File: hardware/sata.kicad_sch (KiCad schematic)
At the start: 36 parts, among them IC1 ASM1061, J9 SATA_22pin, Q2 FDS4435BZ, Q3 FDS4435BZ, Q5 2N7002, Q6 2N7002, Y1 25MHz

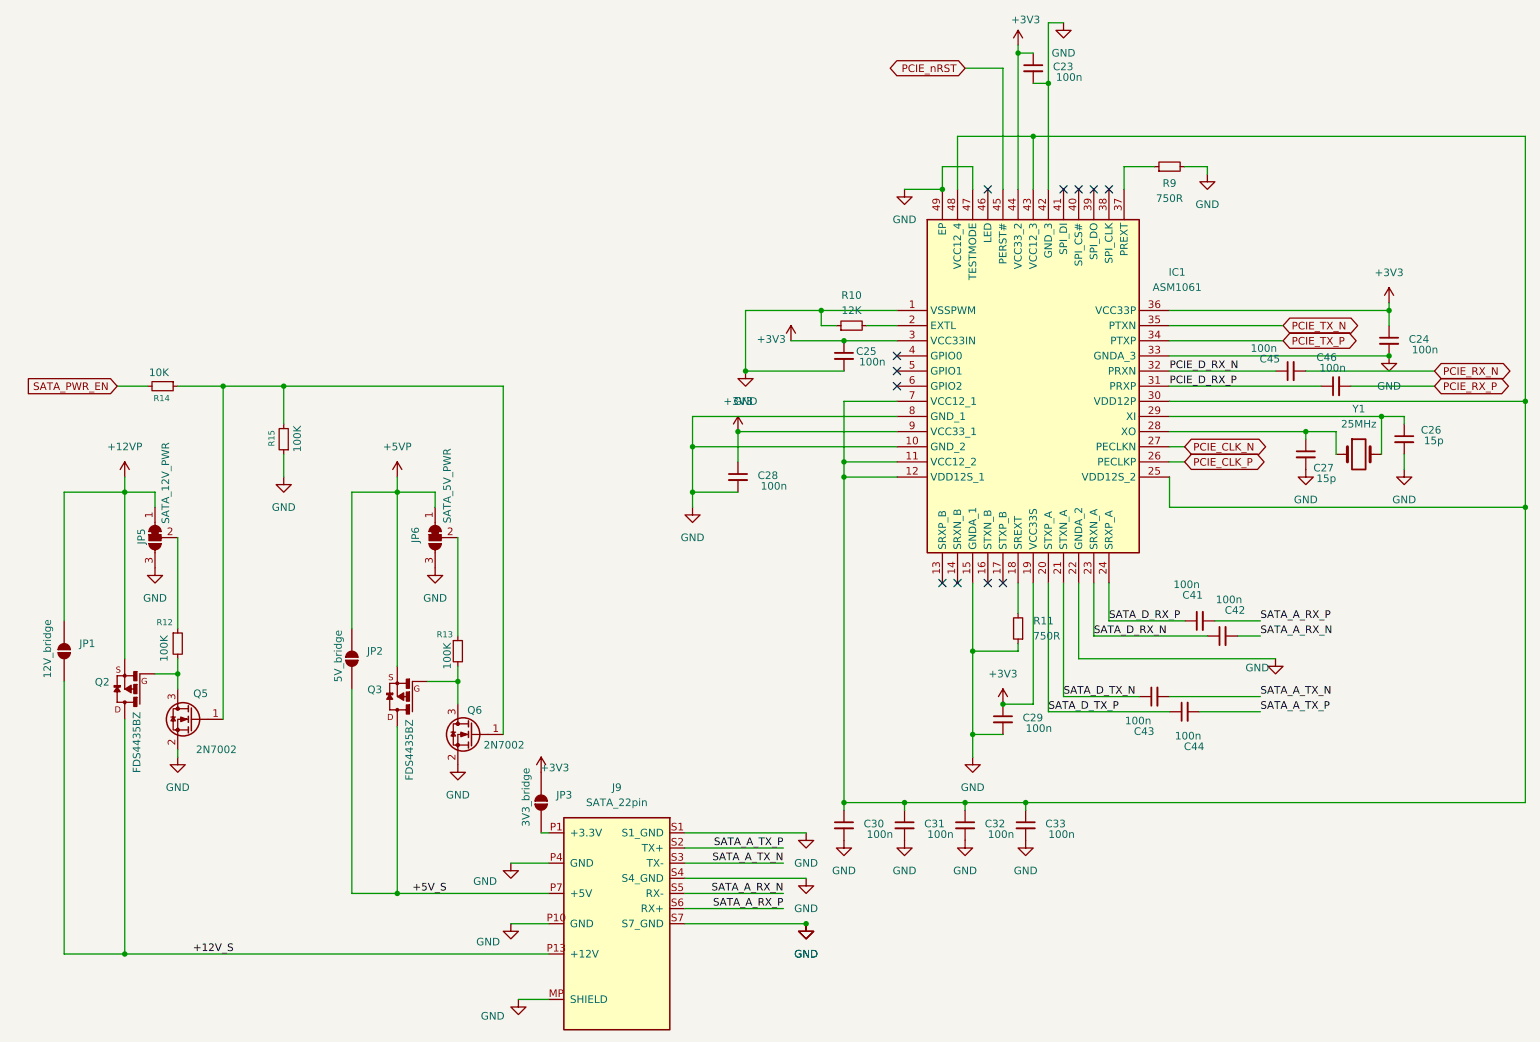
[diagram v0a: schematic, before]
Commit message: refactor: reannotate PCB by position + rename IC1 to U prefix
All reference designators renumbered top-to-bottom, left-to-right.
ASM1061 changed from IC to U prefix.
ERC: 0 errors. DRC: 0 violations. Parity: 0 issues.
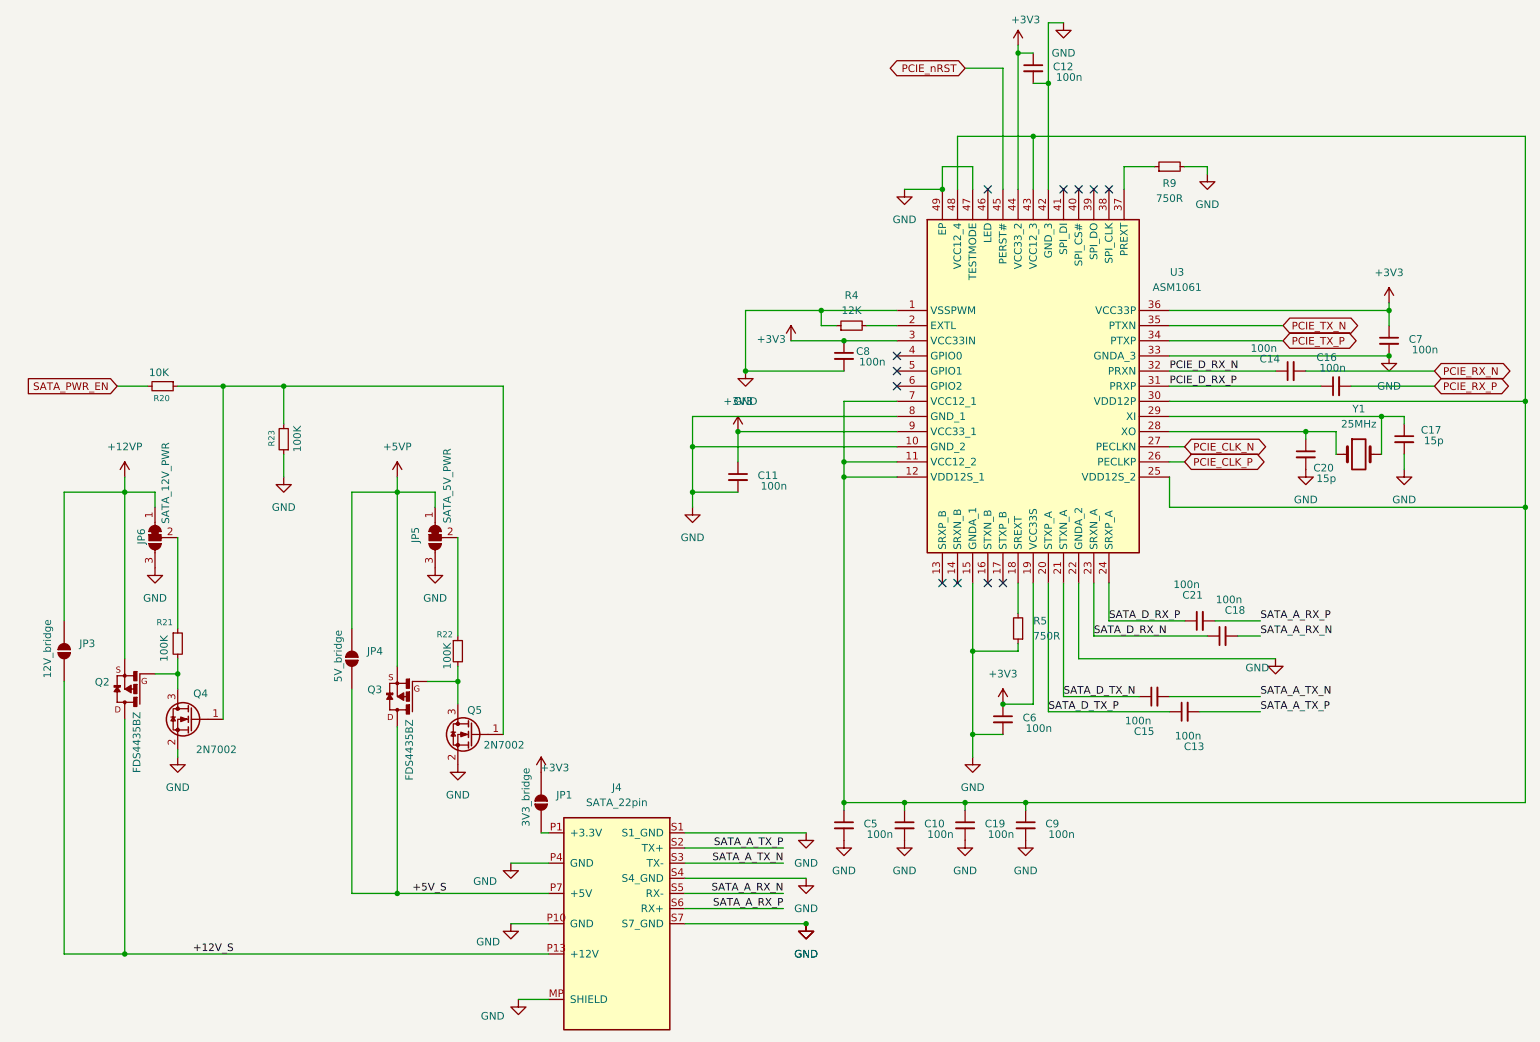
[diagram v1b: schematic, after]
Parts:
- C10: renamed from C31; KiLib_Generator (none) -> SMD_2terminal_chip_molded
- C11: renamed from C28; KiLib_Generator (none) -> SMD_2terminal_chip_molded
- C12: renamed from C23; KiLib_Generator (none) -> SMD_2terminal_chip_molded
- C13: renamed from C44; KiLib_Generator (none) -> SMD_2terminal_chip_molded
- C14: renamed from C45; KiLib_Generator (none) -> SMD_2terminal_chip_molded
- C15: renamed from C43; KiLib_Generator (none) -> SMD_2terminal_chip_molded
- C16: renamed from C46; KiLib_Generator (none) -> SMD_2terminal_chip_molded
- C17: renamed from C26; KiLib_Generator (none) -> SMD_2terminal_chip_molded
- C18: renamed from C42; KiLib_Generator (none) -> SMD_2terminal_chip_molded
- C19: renamed from C32; KiLib_Generator (none) -> SMD_2terminal_chip_molded
- C20: renamed from C27; KiLib_Generator (none) -> SMD_2terminal_chip_molded
- C21: renamed from C41; KiLib_Generator (none) -> SMD_2terminal_chip_molded
- C5: renamed from C30; KiLib_Generator (none) -> SMD_2terminal_chip_molded
- C6: renamed from C29; KiLib_Generator (none) -> SMD_2terminal_chip_molded
- C7: renamed from C24; KiLib_Generator (none) -> SMD_2terminal_chip_molded
- C8: renamed from C25; KiLib_Generator (none) -> SMD_2terminal_chip_molded
- C9: renamed from C33; KiLib_Generator (none) -> SMD_2terminal_chip_molded
- Q4: renamed from Q5; KiLib_Generator (none) -> package/gullwing
- Q5: renamed from Q6; KiLib_Generator (none) -> package/gullwing
- R20: renamed from R14; KiLib_Generator (none) -> SMD_2terminal_chip_molded
- R21: renamed from R12; KiLib_Generator (none) -> SMD_2terminal_chip_molded
- R22: renamed from R13; KiLib_Generator (none) -> SMD_2terminal_chip_molded
- R23: renamed from R15; KiLib_Generator (none) -> SMD_2terminal_chip_molded
- R4: renamed from R10; KiLib_Generator (none) -> SMD_2terminal_chip_molded
- R5: renamed from R11; KiLib_Generator (none) -> SMD_2terminal_chip_molded
- R9: KiLib_Generator (none) -> SMD_2terminal_chip_molded
- renumbered J9 to J4, JP3 to JP1, JP1 to JP3, JP2 to JP4, JP6 to JP5, JP5 to JP6, IC1 to U3

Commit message: feat: add InvenTree IPN field to all schematic symbols
102 components mapped to 41 unique InvenTree part numbers.
IPN format: category prefix + sequential number (e.g. C-001, R-002, U-009).
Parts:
- C10, C11, C12, C13, C14, C15, C16, C18, C19, C21, C5, C6, C7, C8, C9: IPN (none) -> C-001
- C17, C20: IPN (none) -> C-002
- J4: IPN (none) -> J-007
- Q2, Q3: IPN (none) -> Q-001
- Q4, Q5: IPN (none) -> Q-003
- R20: IPN (none) -> R-002
- R21, R22, R23: IPN (none) -> R-004
- R4: IPN (none) -> R-007
- R5, R9: IPN (none) -> R-020
- U3: IPN (none) -> U-009
- Y1: IPN (none) -> Y-003

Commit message: chore: remove redundant supplier fields, keep IPN as single link to InvenTree
Removed: Supplier, Digikey, Notes, KiLib_Generator, Mouser, Arrow fields.
InvenTree IPN is now the only external reference in the schematic.
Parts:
- C10, C11, C12, C13, C14, C15, C16, C17, C18, C19, C20, C21, C5, C6, C7, C8, C9: Digikey 1276-1180-1-ND -> (none); KiLib_Generator SMD_2terminal_chip_molded -> (none); Notes 10% 16V Ceramic Capacitor X7R -> (none); Supplier https://www.digikey.ch/de/products/detail/samsung-electro-m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 -> (none)
- Q2, Q3: IPN Q-001 -> (none); Supplier https://www.digikey.ch/de/products/detail/onsemi/FDS4435BZ/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 -> (none)
- Q4, Q5: IPN Q-003 -> (none); KiLib_Generator package/gullwing -> (none)
- R20, R21, R22, R23, R4, R5, R9: KiLib_Generator SMD_2terminal_chip_molded -> (none)
- U3: IPN U-009 -> (none)

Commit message: feat: complete IPN assignment for all BOM parts
All components now have InvenTree IPN field.
Added IPN to granit library symbols (ASM1061, FDS4435BZ, AP64501).
Added Q-003 to 2N7002 instances.
Only TestPoints have no IPN (not purchaseable).
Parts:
- Q2, Q3: IPN (none) -> Q-001
- Q4, Q5: IPN (none) -> Q-003
- U3: IPN (none) -> U-009
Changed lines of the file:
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@@
 			)
 		)
+		(property "IPN" "Q-003"
+			(at 88.9 135.89 0)
+			(hide yes)
+			(show_name no)
+			(do_not_autoplace no)
+			(effects
+				(font
+					(size 1.27 1.27)
+				)
+			)
+		)
 		(pin "2"
 		)
@@
 			)
 		)
+		(property "IPN" "Q-001"
+			(at 76.2 129.54 0)
+			(hide yes)
+			(show_name no)
+			(do_not_autoplace no)
+			(effects
+				(font
+					(size 1.27 1.27)
+				)
+			)
+		)
 		(pin "1-3"
 		)
@@
 			)
 		)
+		(property "IPN" "U-009"
+			(at 160.02 64.77 0)
+			(hide yes)
+			(show_name no)
+			(do_not_autoplace no)
+			(effects
+				(font
+					(size 1.27 1.27)
+				)
+			)
+		)
 		(pin "26"
 		)
@@
 			)
 		)
+		(property "IPN" "Q-001"
+			(at 30.48 128.27 0)
+			(hide yes)
+			(show_name no)
+			(do_not_autoplace no)
+			(effects
+				(font
+					(size 1.27 1.27)
+				)
+			)
+		)
 		(pin "5-8"
 		)
@@
 			(at 41.91 133.35 0)
 			(hide yes)
+			(show_name no)
+			(do_not_autoplace no)
+			(effects
+				(font
+					(size 1.27 1.27)
+				)
+			)
+		)
+		(property "IPN" "Q-003"
+			(at 41.91 133.35 0)
+			(hide yes)

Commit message: fix: restore SATA TX+ pin number to S2 (was corrupted by HR911130A shield pin remap)
ERC: 0 errors, 0 warnings
DRC: 0 violations, 0 parity issues
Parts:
- J4: IPN J-007 -> (none)
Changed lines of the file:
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@@
-			)
-		)
-		(property "IPN" "J-007"
-			(at 0 0 0)
-			(hide yes)
-			(show_name no)
-			(do_not_autoplace no)
-			(effects
-				(font
-					(size 1.27 1.27)
-				)
 			)
 		)
@@
 		(pin "P4"
 		)
-		(pin "S2"
+		(pin "S1"
 		)
 		(pin "S3"
@@
 		(pin "P15"
 		)
-		(pin "S1"
+		(pin "S2"
 		)
 		(pin "P3"

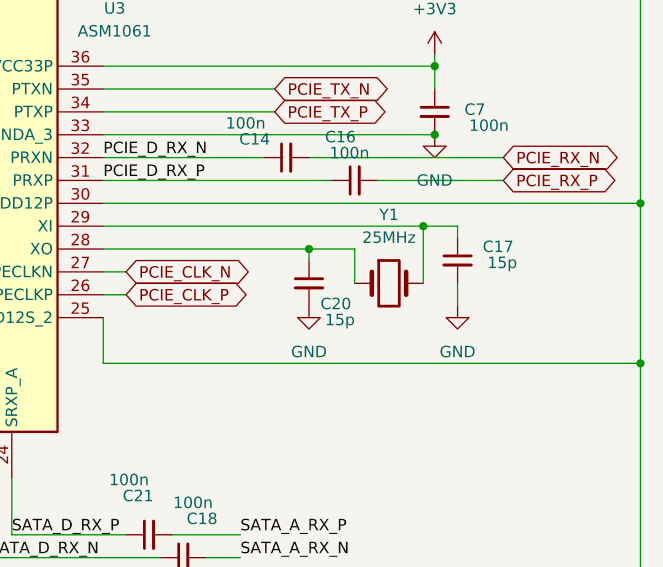
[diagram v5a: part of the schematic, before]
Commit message: feat: swap crystal Y1 to 2016 4-pin (easier to source)
Changed from Crystal_SMD_3215-2Pin to Crystal_SMD_2016-4Pin_2.0x1.6mm.
Re-routed PCIe area around new crystal placement.
ERC: 0 errors, 0 warnings. DRC: 0 violations.
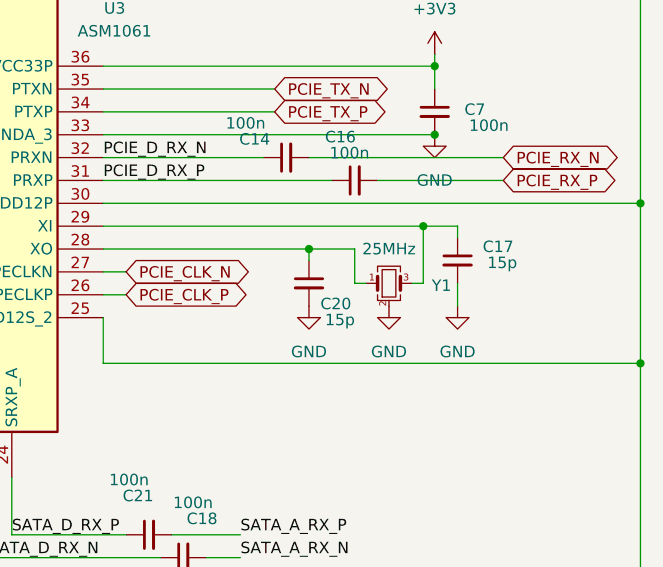
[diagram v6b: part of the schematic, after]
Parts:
- removed Y1: 25MHz, Crystal:Crystal_SMD_3215-2Pin_3.2x1.5mm, symbol Device:Crystal
- added Y1: 25MHz, Crystal:Crystal_SMD_2016-4Pin_2.0x1.6mm, symbol Device:Crystal_GND24_Small
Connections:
- net GND: now also Y1.2 (G), Y1.4 (G)
- net at C17.1, U3.29 (XI): now also Y1.3
- net at C20.1, U3.28 (XO): now also Y1.1
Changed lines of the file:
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@@
 	(wire
 		(pts
+			(xy 233.68 88.9) (xy 234.95 88.9)
+		)
+		(stroke
+			(width 0)
+			(type default)
+		)
+	)
+	(wire
+		(pts
 			(xy 161.29 147.32) (xy 151.13 147.32)
 		)
@@
 	(wire
 		(pts
+			(xy 240.03 88.9) (xy 241.3 88.9)
+		)
+		(stroke
+			(width 0)
+			(type default)
+		)
+	)
+	(wire
+		(pts
 			(xy 265.43 80.01) (xy 265.43 97.79)
 		)
@@
 	)
 	(symbol
-		(lib_id "Device:Crystal")
-		(at 237.49 88.9 0)
-		(unit 1)
-		(body_style 1)
-		(exclude_from_sim no)
-		(in_bom yes)
-		(on_board yes)
-		(in_pos_files yes)
-		(dnp no)
-		(fields_autoplaced yes)
-		(property "Reference" "Y1"
-			(at 237.49 81.28 0)
-			(show_name no)
-			(do_not_autoplace no)
-			(effects
-				(font
-					(size 1.27 1.27)
-				)
-			)
-		)
-		(property "Value" "25MHz"
-			(at 237.49 83.82 0)
-			(show_name no)
-			(do_not_autoplace no)
-			(effects
-				(font
-					(size 1.27 1.27)
-				)
-			)
-		)
-		(property "Footprint" "Crystal:Crystal_SMD_3215-2Pin_3.2x1.5mm"
-			(at 237.49 88.9 0)
-			(hide yes)
-			(show_name no)
-			(do_not_autoplace no)
-			(effects
-				(font
-					(size 1.27 1.27)
-				)
-			)
-		)
-		(property "Datasheet" ""
-			(at 237.49 88.9 0)
-			(hide yes)
-			(show_name no)
-			(do_not_autoplace no)
-			(effects
-				(font
-					(size 1.27 1.27)
-				)
-			)
-		)
-		(property "Description" "Two pin crystal"
-			(at 237.49 88.9 0)
-			(hide yes)
-			(show_name no)
-			(do_not_autoplace no)
-			(effects
-				(font
-					(size 1.27 1.27)
-				)
-			)
-		)
-		(property "IPN" "Y-003"
-			(at 0 0 0)
-			(hide yes)
-			(show_name no)
-			(do_not_autoplace no)
-			(effects
-				(font
-					(size 1.27 1.27)
-				)
-			)
-		)
-		(pin "1"
-		)
-		(pin "2"
-		)
-		(instances
-			(project "granit"
-				(path "/d2c135e3-a983-4cd4-8cff-b50ca3c7671a/b486f39b-2401-4245-9dd6-e411236f99dc"
-					(reference "Y1")
-					(unit 1)
-				)
-			)
-		)
-	)
-	(symbol
 		(lib_id "Device:R_Small")
 		(at 152.4 67.31 90)
@@
 	)
 	(symbol
+		(lib_id "Device:Crystal_GND24_Small")
+		(at 237.49 88.9 0)
+		(unit 1)
+		(body_style 1)
+		(exclude_from_sim no)
+		(in_bom yes)
+		(on_board yes)
+		(in_pos_files yes)
+		(dnp no)
+		(property "Reference" "Y1"
+			(at 243.332 89.154 0)
+			(show_name no)
+			(do_not_autoplace no)
+			(effects
+				(font
+					(size 1.27 1.27)
+				)
+			)
+		)
+		(property "Value" "25MHz"
+			(at 237.49 85.09 0)
+			(show_name no)
+			(do_not_autoplace no)
+			(effects
+				(font
+					(size 1.27 1.27)
+				)
+			)
+		)
+		(property "Footprint" "Crystal:Crystal_SMD_2016-4Pin_2.0x1.6mm"
+			(at 237.49 88.9 0)
+			(hide yes)
+			(show_name no)
+			(do_not_autoplace no)
+			(effects
+				(font
+					(size 1.27 1.27)
+				)
+			)
+		)
+		(property "Datasheet" ""
+			(at 237.49 88.9 0)
+			(hide yes)
+			(show_name no)
+			(do_not_autoplace no)
+			(effects
+				(font
+					(size 1.27 1.27)
+				)
+			)
+		)
+		(property "Description" "Four pin crystal, GND on pins 2 and 4, small symbol"
+			(at 237.49 88.9 0)
+			(hide yes)
+			(show_name no)
+			(do_not_autoplace no)
+			(effects
+				(font
+					(size 1.27 1.27)
+				)
+			)
+		)
+		(property private "KLC_S3.3" "The rectangle is not a symbol body but a graphical element"
+			(at 237.49 99.06 0)
+			(hide yes)
+			(show_name yes)
+			(do_not_autoplace no)
+			(effects
+				(font
+					(size 1.27 1.27)
+				)
+			)
+		)
+		(property private "KLC_S4.1" "Some pins are on 50mil grid to make the symbol small"
+			(at 237.49 101.6 0)
+			(hide yes)
+			(show_name yes)
+			(do_not_autoplace no)
+			(effects
+				(font
+					(size 1.27 1.27)
+				)
+			)
+		)
+		(pin "4"
+		)
+		(pin "1"
+		)
+		(pin "3"
+		)
+		(pin "2"
+		)
+		(instances
+			(project "granit"
+				(path "/d2c135e3-a983-4cd4-8cff-b50ca3c7671a/b486f39b-2401-4245-9dd6-e411236f99dc"
+					(reference "Y1")
+					(unit 1)
+				)
+			)
+		)
+	)
+	(symbol
 		(lib_id "Device:R_Small")
 		(at 39.37 120.65 0)
@@
 					(unit 1)
 				)
+			)
+		)
+	)
+	(symbol
+		(lib_id "power:GND")
+		(at 237.49 91.44 0)
+		(unit 1)
+		(body_style 1)
+		(exclude_from_sim no)
+		(in_bom yes)
+		(on_board yes)
+		(in_pos_files yes)
+		(dnp no)
+		(fields_autoplaced yes)
+		(property "Reference" "#PWR093"
+			(at 237.49 97.79 0)
+			(hide yes)
+			(show_name no)
+			(do_not_autoplace no)
+			(effects
+				(font
+					(size 1.27 1.27)
+				)
+			)
+		)
+		(property "Value" "GND"
+			(at 237.49 96.52 0)
+			(show_name no)
+			(do_not_autoplace no)
+			(effects
+				(font
+					(size 1.27 1.27)
+				)
+			)
+		)
+		(property "Footprint" ""
+			(at 237.49 91.44 0)
+			(hide yes)
+			(show_name no)
+			(do_not_autoplace no)
+			(effects
+				(font
+					(size 1.27 1.27)
+				)
+			)
+		)
+		(property "Datasheet" ""
+			(at 237.49 91.44 0)
+			(hide yes)
+			(show_name no)
+			(do_not_autoplace no)
+			(effects
+				(font
+					(size 1.27 1.27)
+				)
+			)
+		)
+		(property "Description" "Power symbol creates a global label with name \"GND\" , ground"
+			(at 237.49 91.44 0)
+			(hide yes)
+			(show_name no)
+			(do_not_autoplace no)
+			(effects
+				(font
+					(size 1.27 1.27)
+				)
+			)
+		)
+		(pin "1"
+		)
+		(instances
+			(project "granit"
+				(path "/d2c135e3-a983-4cd4-8cff-b50ca3c7671a/b486f39b-2401-4245-9dd6-e411236f99dc"
+					(reference "#PWR093")
+					(unit 1)
+				)

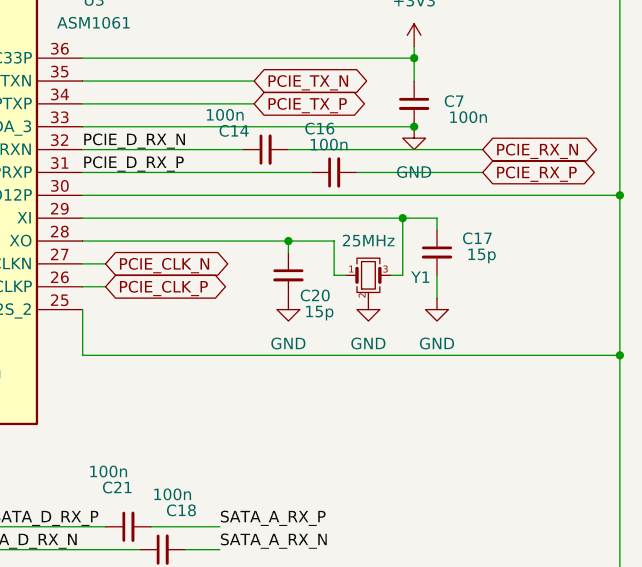
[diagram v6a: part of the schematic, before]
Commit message: fix: change crystal load caps from 15pF to 18pF (matches 12pF load spec)
C17, C20: 15pF → 18pF (C-015, CML0805C0G180JT50V)
C_load = (18×18)/(18+18) + 3pF stray = 12pF ✅
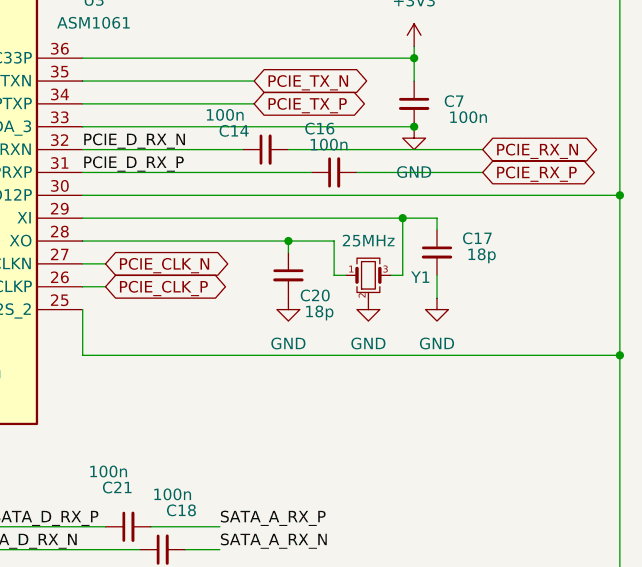
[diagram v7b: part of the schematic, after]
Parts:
- C17, C20: value 15p -> 18p; IPN C-002 -> C-015
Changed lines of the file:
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@@
 			)
 		)
-		(property "Value" "15p"
+		(property "Value" "18p"
 			(at 248.412 86.614 0)
 			(show_name no)
@@
 			)
 		)
-		(property "IPN" "C-002"
+		(property "IPN" "C-015"
 			(at 0 0 0)
 			(hide yes)
@@
 			)
 		)
-		(property "Value" "15p"
+		(property "Value" "18p"
 			(at 230.378 92.964 0)
 			(show_name no)
@@
 			)
 		)
-		(property "IPN" "C-002"
+		(property "IPN" "C-015"
 			(at 0 0 0)
 			(hide yes)

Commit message: fix: add missing IPNs for J4 (SATA), J5 (HR911130A), Y1 (crystal)
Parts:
- J4: IPN (none) -> J-007
- Y1: IPN (none) -> Y-003
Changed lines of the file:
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@@
 			)
 		)
+		(property "IPN" "J-007"
+			(at 114.3 165.1 0)
+			(hide yes)
+			(show_name no)
+			(do_not_autoplace no)
+			(effects
+				(font
+					(size 1.27 1.27)
+				)
+			)
+		)
 		(pin "P12"
 		)
@@
 			(do_not_autoplace no)
 			(effects
+				(font
+					(size 1.27 1.27)
+				)
+			)
+		)
+		(property "IPN" "Y-003"
+			(at 237.49 88.9 0)
+			(hide yes)
+			(show_name no)
+			(do_not_autoplace no)
+			(effects
